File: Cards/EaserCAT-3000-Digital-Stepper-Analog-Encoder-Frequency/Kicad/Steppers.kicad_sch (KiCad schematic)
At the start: 15 parts, among them J10 Encoder, J11 Step1, J11 Step3, J13 Step2, J13 Step4, J17 THCAD, U1 MAX3485CSA/ESA, U2 TXS0108EPW

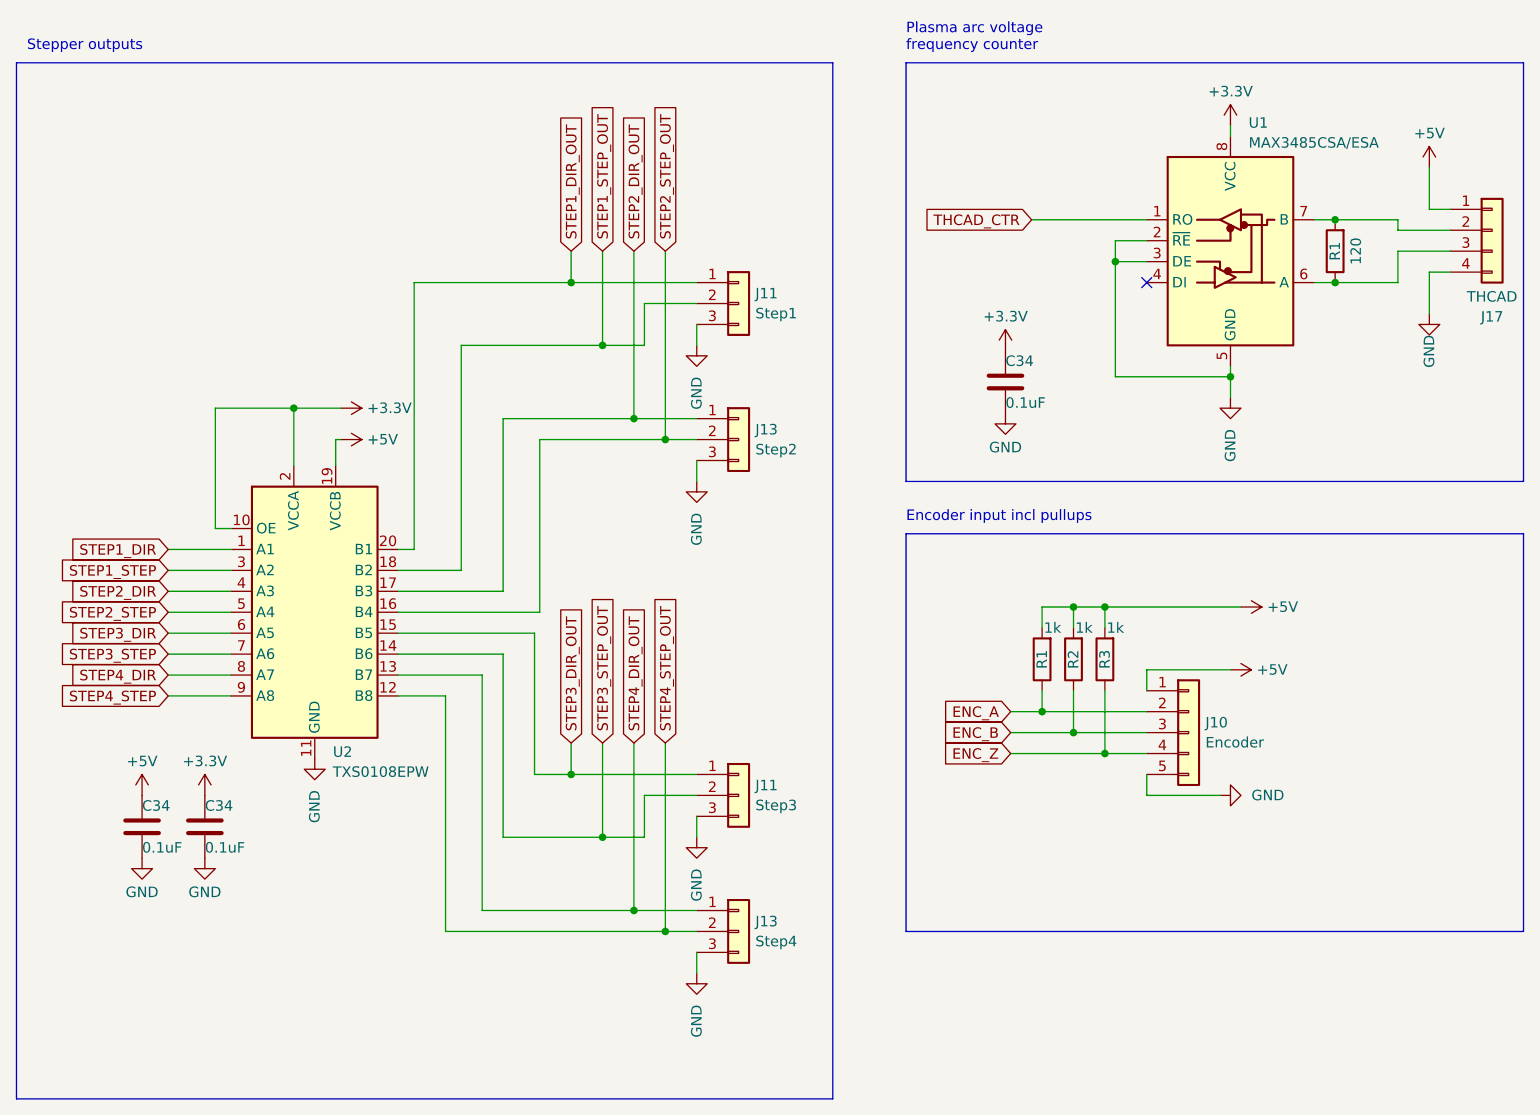
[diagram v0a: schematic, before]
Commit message: Moving all to Kicad8. Housekeeping symbols,libraries,3d-models
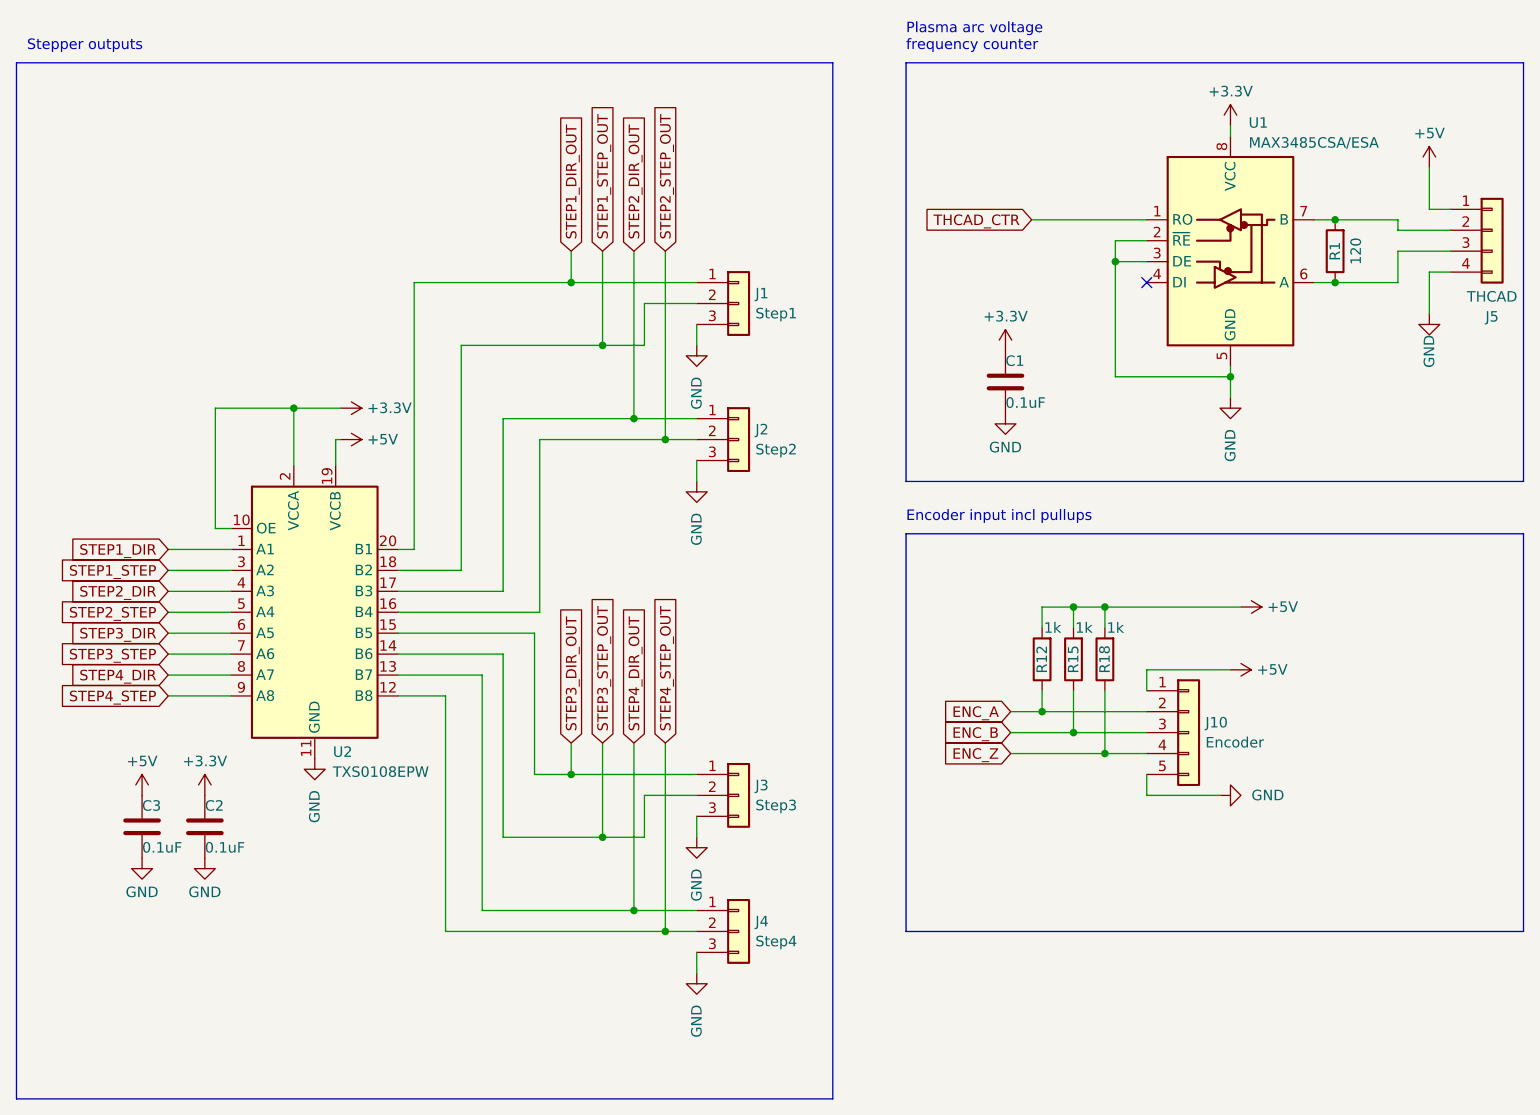
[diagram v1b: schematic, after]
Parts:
- renumbered C34 to C1, C34 to C2, C34 to C3, J11 to J1, J13 to J2, J11 to J3, J13 to J4, J17 to J5, R1 to R12, R2 to R15, R3 to R18
